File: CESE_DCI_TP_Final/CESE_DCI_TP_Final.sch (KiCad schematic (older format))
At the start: 50 parts, among them J1 Signal Inputs, J2 12V POWER, J3 POWER, M1 Motor 12V CC, Q1 BC337, Q1 IRFZ44NS, Q2 BC337, Q2 IRFZ44NS, Q3 IRFZ44NS, Q4 IRFZ44NS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

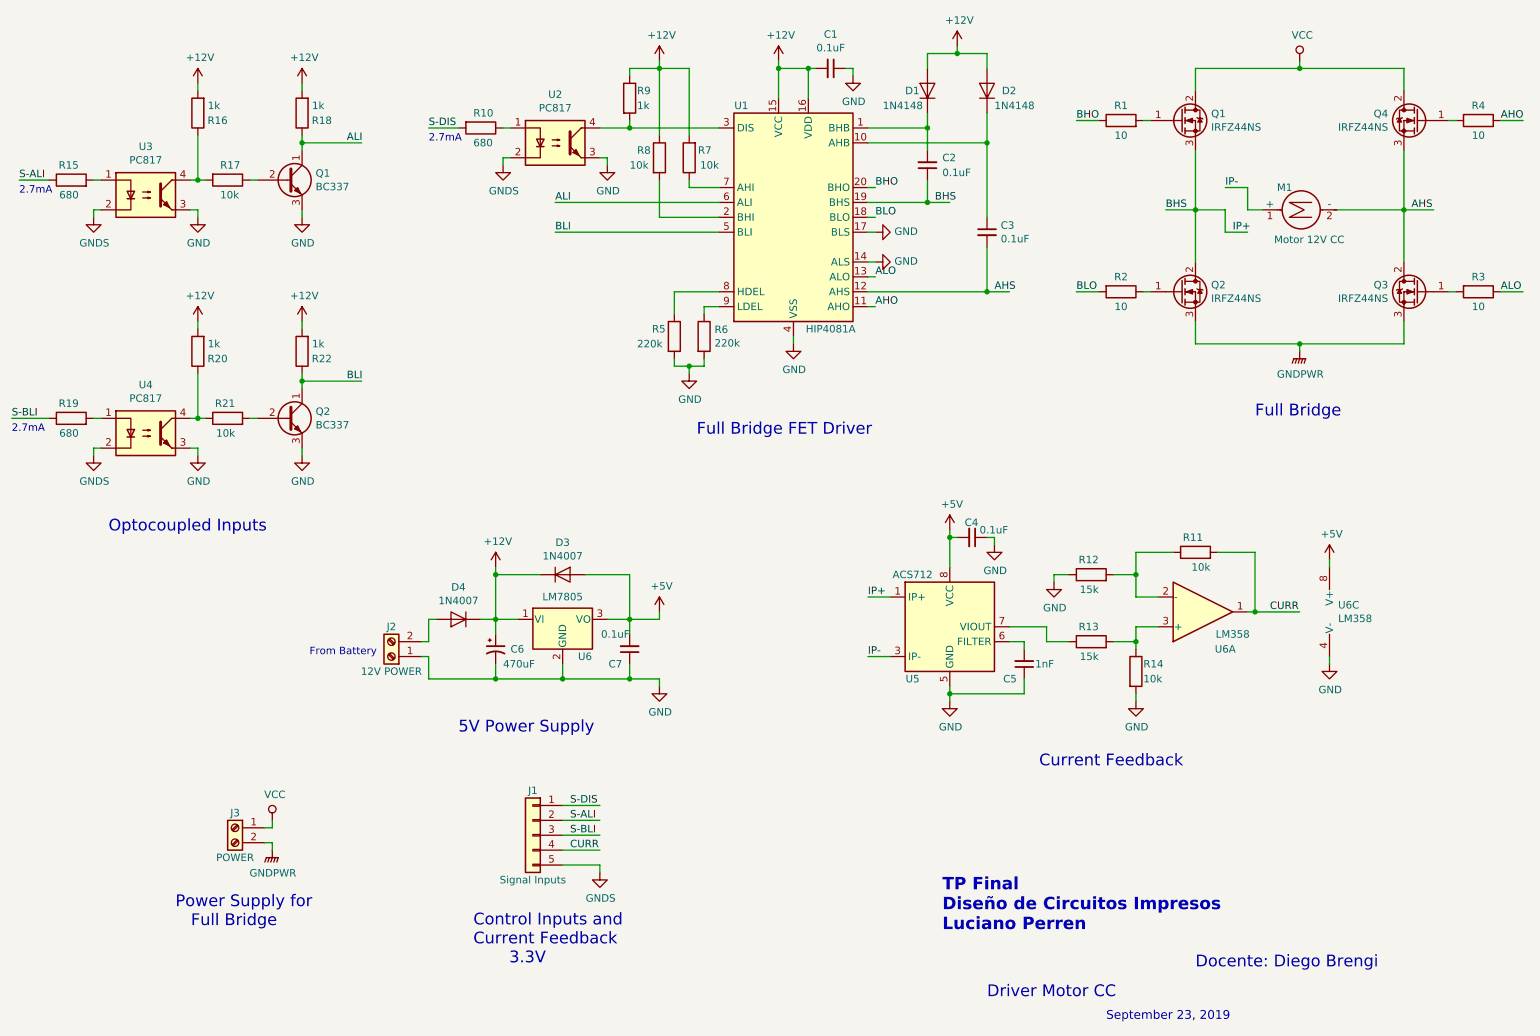
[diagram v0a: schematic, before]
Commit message: Se actualizo el esquematico
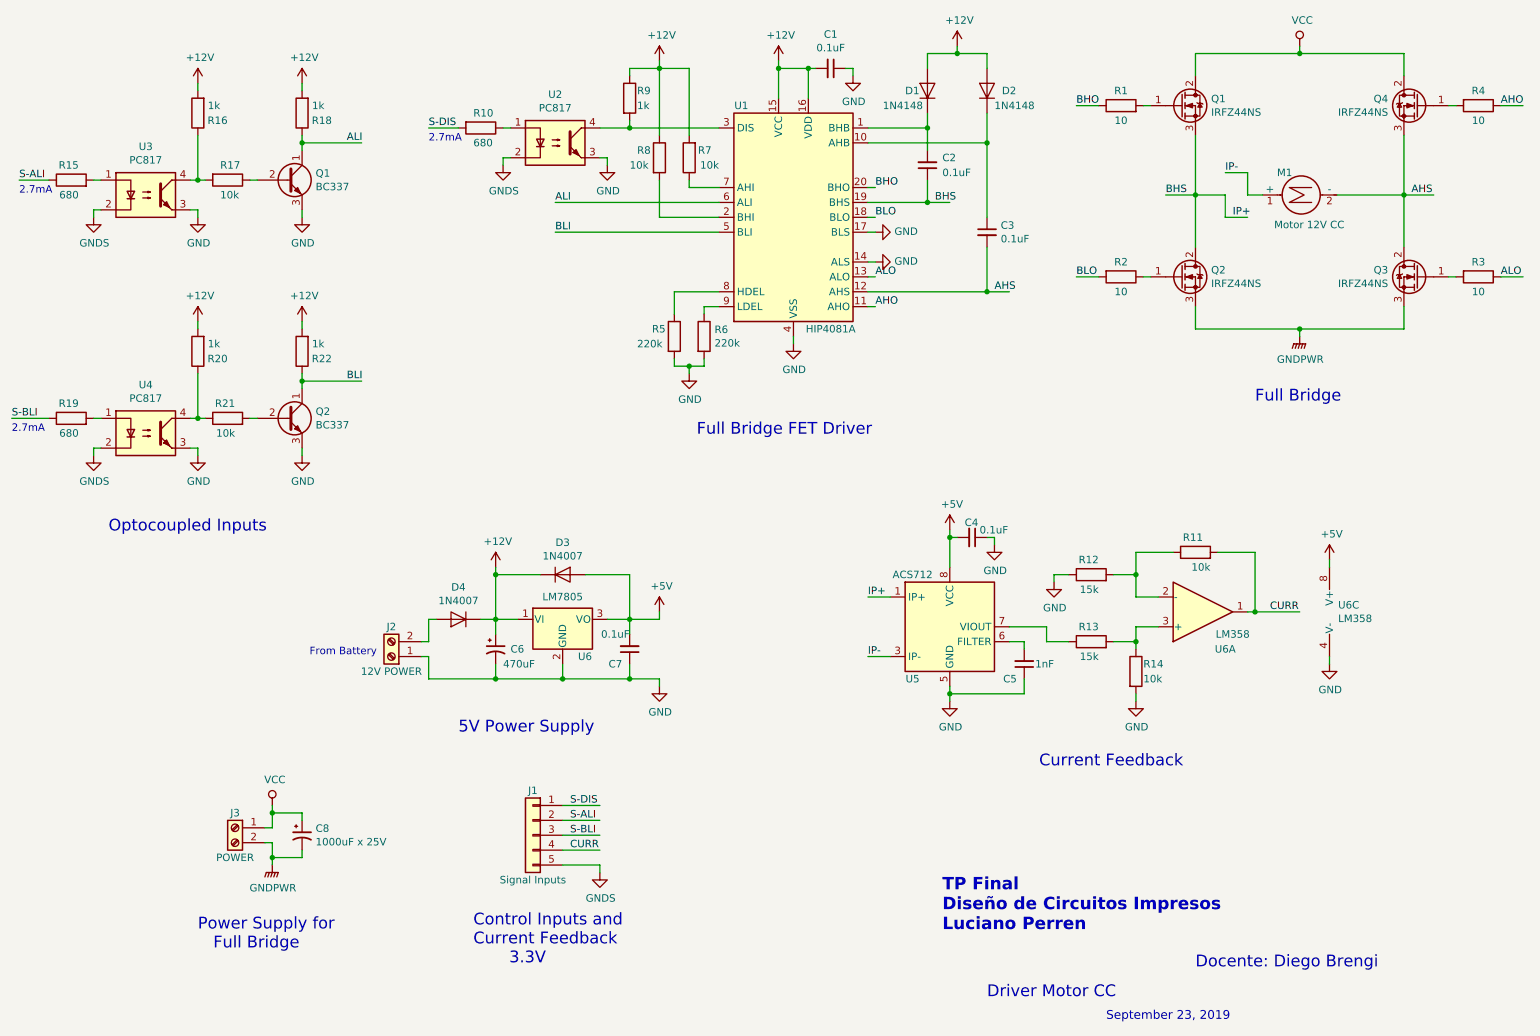
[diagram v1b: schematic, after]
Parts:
- added C8: 1000uF x 25V, symbol Device:CP1_Small
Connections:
- wire segments 193 -> 199
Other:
- moved on the sheet: M1, Q1, Q2, Q3, Q4, R1, R2, R3, R4

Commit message: Se realizaron correcciones en el .sch
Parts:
- removed Q1: BC337, Package_TO_SOT_THT:TO-92_Inline, symbol Transistor_BJT:BC337
- added Q5: BC337, Package_TO_SOT_THT:TO-92_Inline, symbol Transistor_BJT:BC337
- renumbered Q2 to Q6, U6 to U7

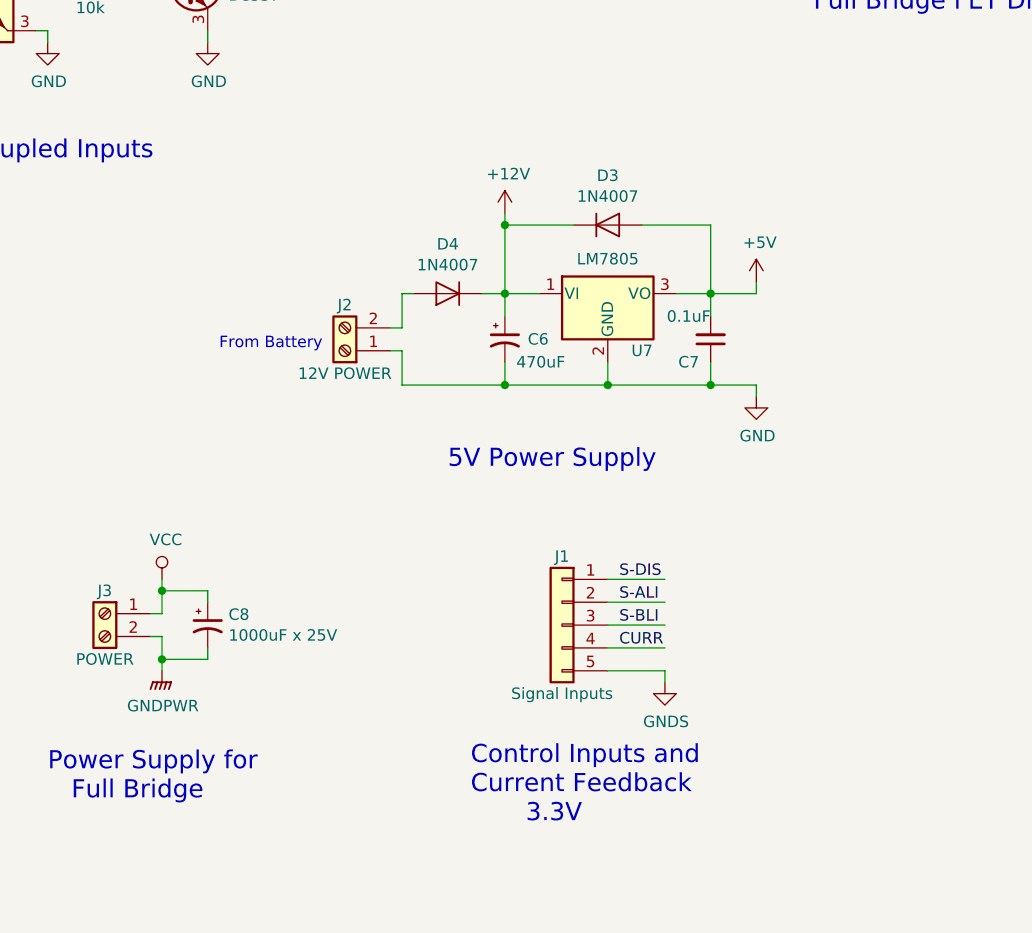
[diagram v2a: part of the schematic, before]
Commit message: Se corrijen errores ERC
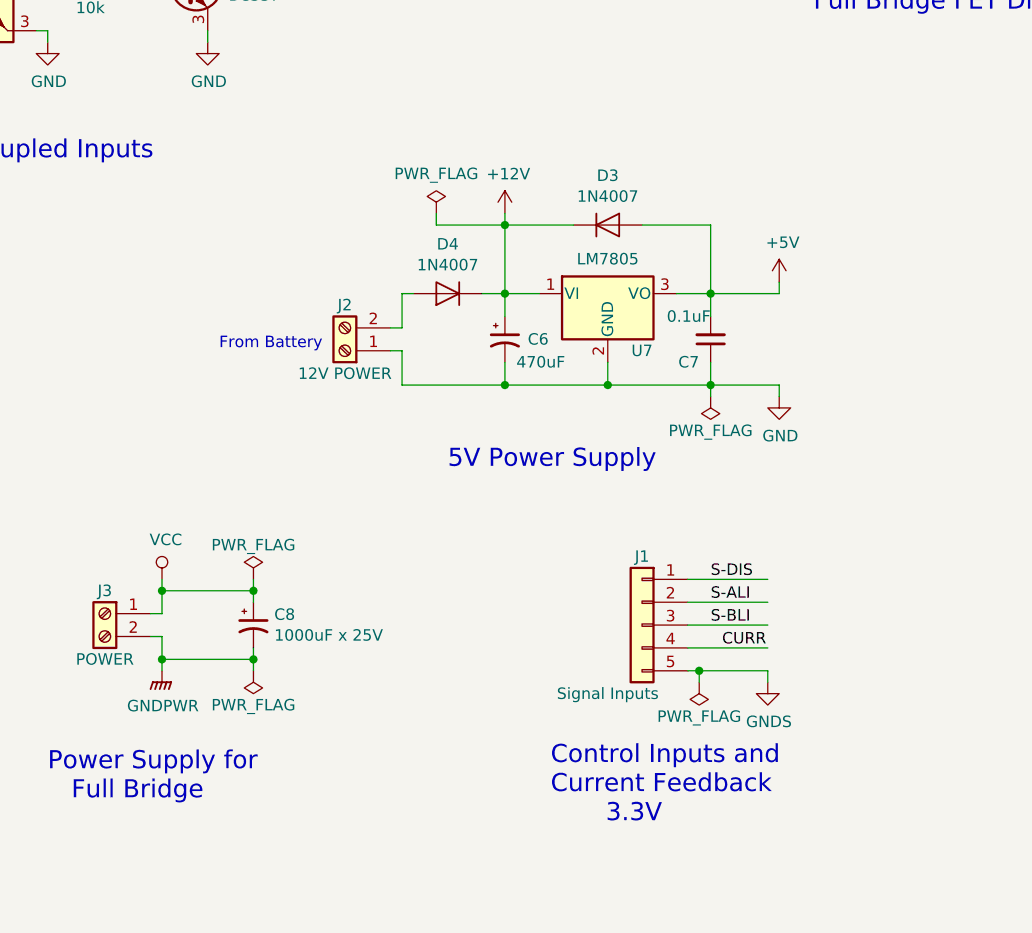
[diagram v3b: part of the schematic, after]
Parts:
- C1, C2, C3, C4, C5, C7: footprint (none) -> Capacitor_SMD:C_1206_3216Metric_Pad1.42x1.75mm_HandSolder
- C6: footprint (none) -> Capacitor_THT:CP_Radial_D10.0mm_P5.00mm
- C8: footprint (none) -> Capacitor_THT:CP_Radial_D16.0mm_P7.50mm
- J1: footprint (none) -> Connector_PinHeader_2.54mm:PinHeader_1x05_P2.54mm_Vertical
- J2, J3, M1: footprint (none) -> TerminalBlock_Phoenix:TerminalBlock_Phoenix_MKDS-1,5-2-5.08_1x02_P5.08mm_Horizontal
- Q1, Q2, Q3, Q4: footprint Package_TO_SOT_THT:TO-220-3_Vertical -> Package_TO_SOT_SMD:TO-263-3_TabPin2
- R1, R10, R11, R12, R13, R14, R15, R16, R17, R18, R19, R2, R20, R21, R22, R3, R4, R5, R6, R7, R8, R9: footprint (none) -> Resistor_SMD:R_1206_3216Metric_Pad1.42x1.75mm_HandSolder
- U1: footprint (none) -> Package_DIP:DIP-20_W7.62mm_Socket
- U6: footprint (none) -> Package_SO:SOIC-8-1EP_3.9x4.9mm_P1.27mm_EP2.35x2.35mm
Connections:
- wire segments 199 -> 206
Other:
- moved on the sheet: C8, J1

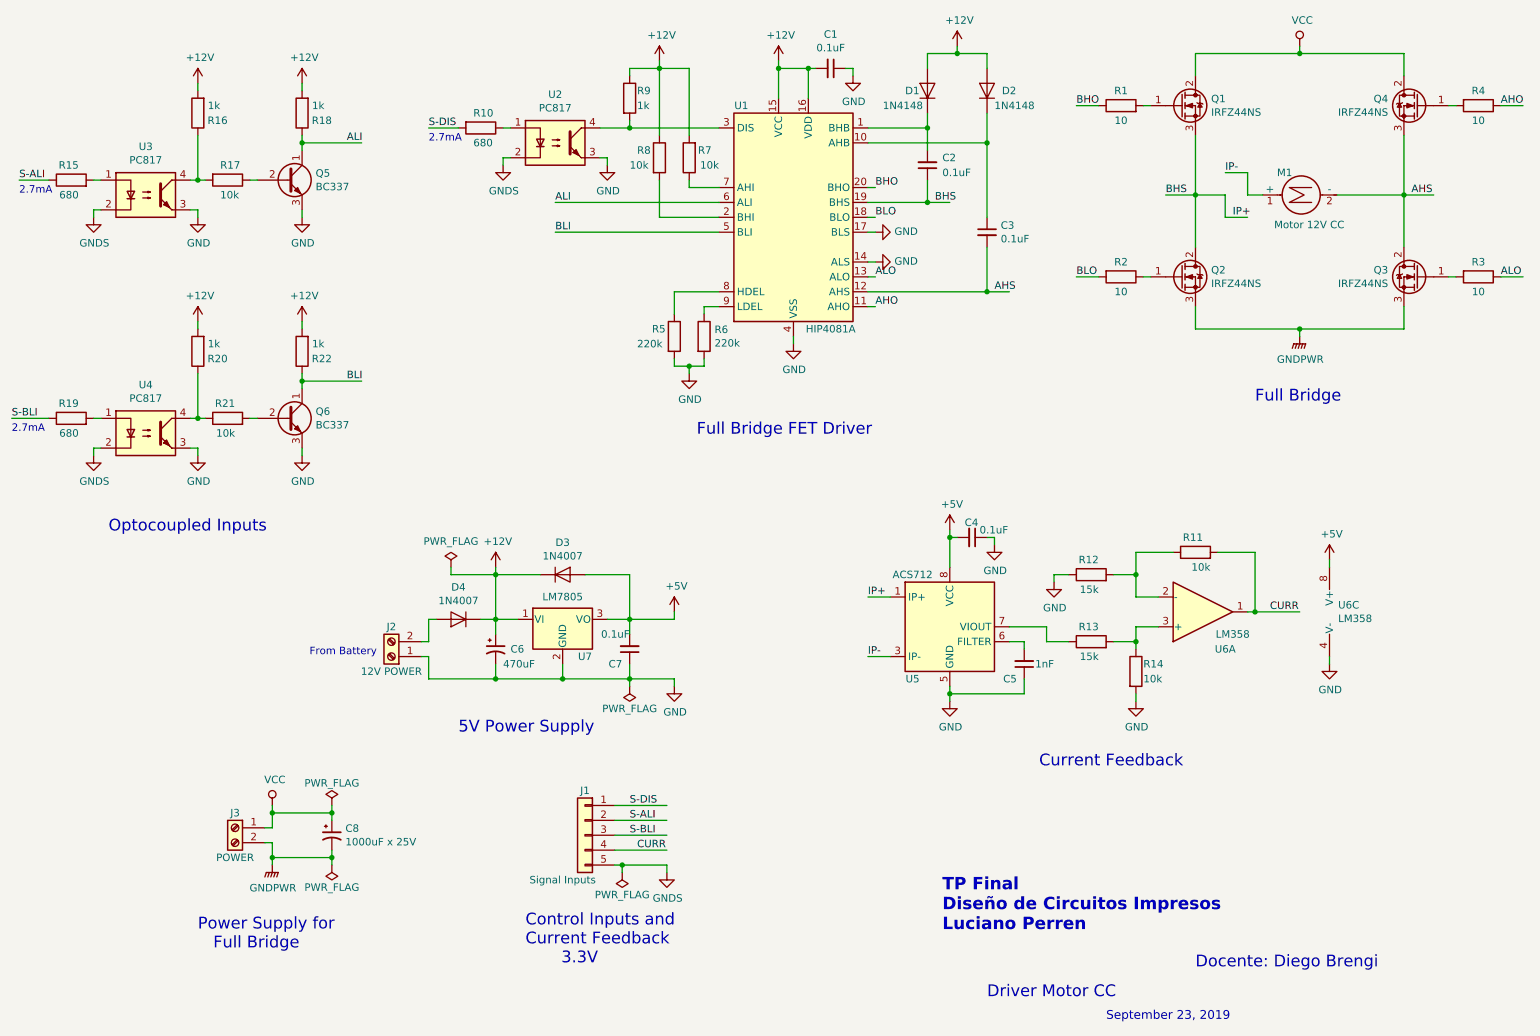
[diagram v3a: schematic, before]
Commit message: Se finaliza PCB + 3D View + BOM
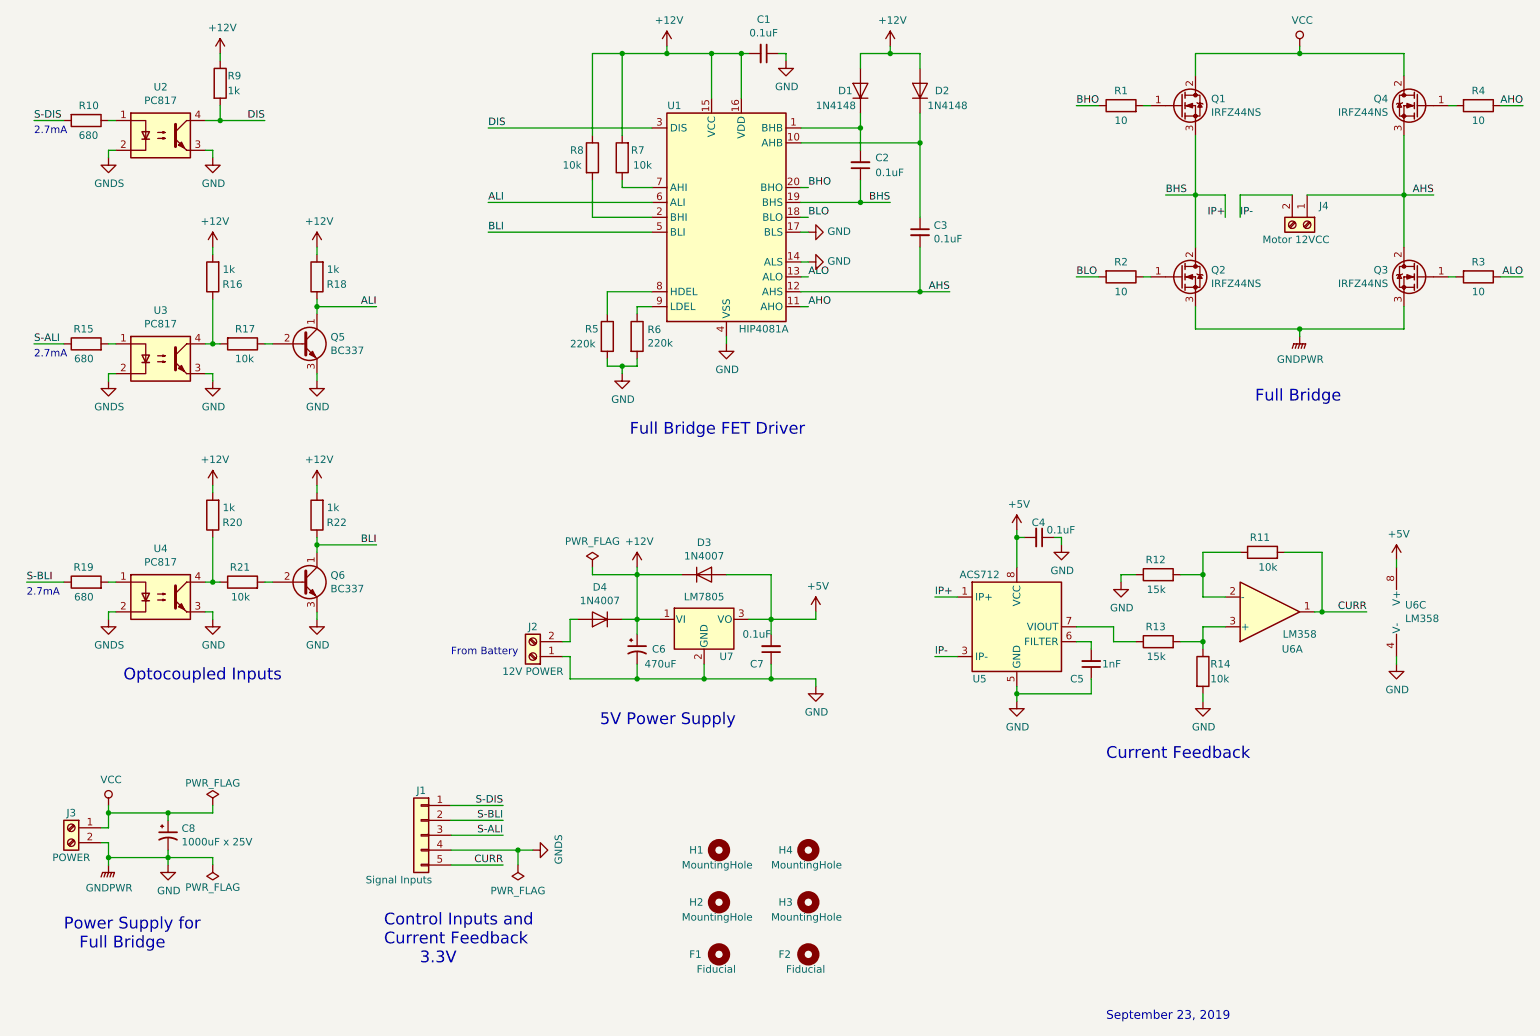
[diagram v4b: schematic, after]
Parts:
- removed M1: Motor 12V CC, TerminalBlock_Phoenix:TerminalBlock_Phoenix_MKDS-1,5-2-5.08_1x02_P5.08mm_Horizontal, symbol Motor:Motor_DC
- added F1, F2: Fiducial, Fiducial:Fiducial_0.5mm_Dia_1mm_Outer, symbol Mechanical:MountingHole
- added H1, H2, H3, H4: MountingHole, MountingHole:MountingHole_2.7mm_M2.5, symbol Mechanical:MountingHole
- added J4: Motor 12VCC, TerminalBlock:TerminalBlock_bornier-2_P5.08mm, symbol Connector:Screw_Terminal_01x02
- C1, C2, C3, C4, C7: Digi-Key Number (none) -> 399-7357-2-ND
- C5: Digi-Key Number (none) -> 399-17173-2-ND
- C6: Digi-Key Number (none) -> P10386TB-ND
- C8: Digi-Key Number (none) -> 493-14604-3-ND
- D1, D2: Digi-Key Number (none) -> 1N4148FS-ND
- D3, D4: Digi-Key Number (none) -> 1N4007FSCT-ND
- J1: Digi-Key Number (none) -> 732-5318-ND
- J2, J3: footprint TerminalBlock_Phoenix:TerminalBlock_Phoenix_MKDS-1,5-2-5.08_1x02_P5.08mm_Horizontal -> TerminalBlock:TerminalBlock_bornier-2_P5.08mm; Digi-Key Number (none) -> A113320-ND
- Q1, Q2, Q3, Q4: footprint Package_TO_SOT_SMD:TO-263-3_TabPin2 -> Package_TO_SOT_SMD:TO-263-2; Digi-Key Number (none) -> IRFZ44NSTRLPBFTR-ND
- Q5, Q6: Digi-Key Number (none) -> BC33725TFRTR-ND
- R1, R2, R3, R4: Digi-Key Number (none) -> CRM1206-FX-10R0ELFCT-ND
- R10, R15, R19: Digi-Key Number (none) -> 311-680FRCT-ND
- R11, R14, R17, R21, R7, R8: Digi-Key Number (none) -> 311-10KERTR-ND
- R12, R13: Digi-Key Number (none) -> A129824TR-ND
- R16, R20, R22, R9: Digi-Key Number (none) -> CR1206-JW-102ELFTR-ND
- R5, R6: Digi-Key Number (none) -> A130566TR-ND
- U1: Digi-Key Number (none) -> HIP4081AIPZ-ND
- U2, U3, U4: Digi-Key Number (none) -> EL817-ND
- U5: Digi-Key Number (none) -> 620-1190-2-ND
- U6: Digi-Key Number (none) -> 497-1591-2-ND
- U7: Digi-Key Number (none) -> 296-47192-ND
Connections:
- net labels added: DIS
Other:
- note removed: "Docente: Diego Brengi"
- note removed: "Driver Motor CC\n"
- note removed: "TP Final\nDiseño de Circuitos Impresos\nLuciano Perren\n"
- moved on the sheet: C1, C2, C3, C4, C5, C6, C7, C8, D1, D2, D3, D4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
